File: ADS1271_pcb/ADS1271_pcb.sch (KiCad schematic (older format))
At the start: 2 parts, among them U1 ADS1271

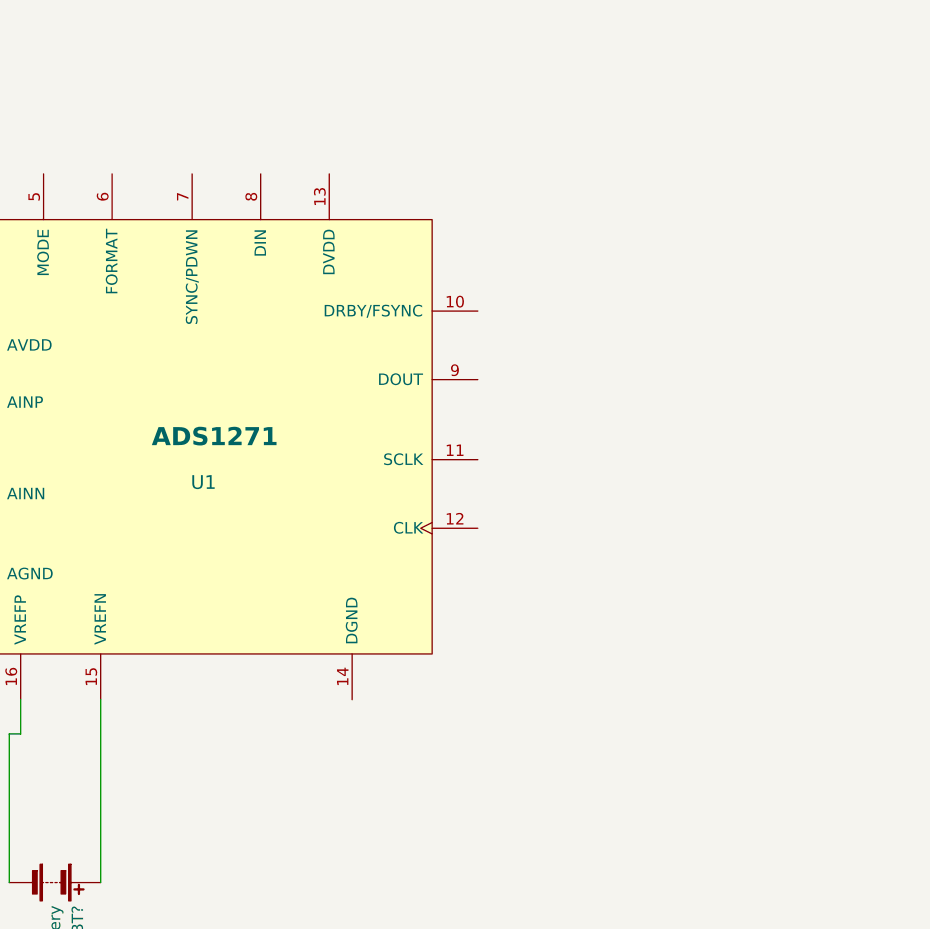
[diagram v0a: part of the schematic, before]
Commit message: Se agrega en el esquematico los labels y resistencias
FALTA: Capacitores de bypass, baterías, y definir funciones del resto de los pines. @lvillarreal
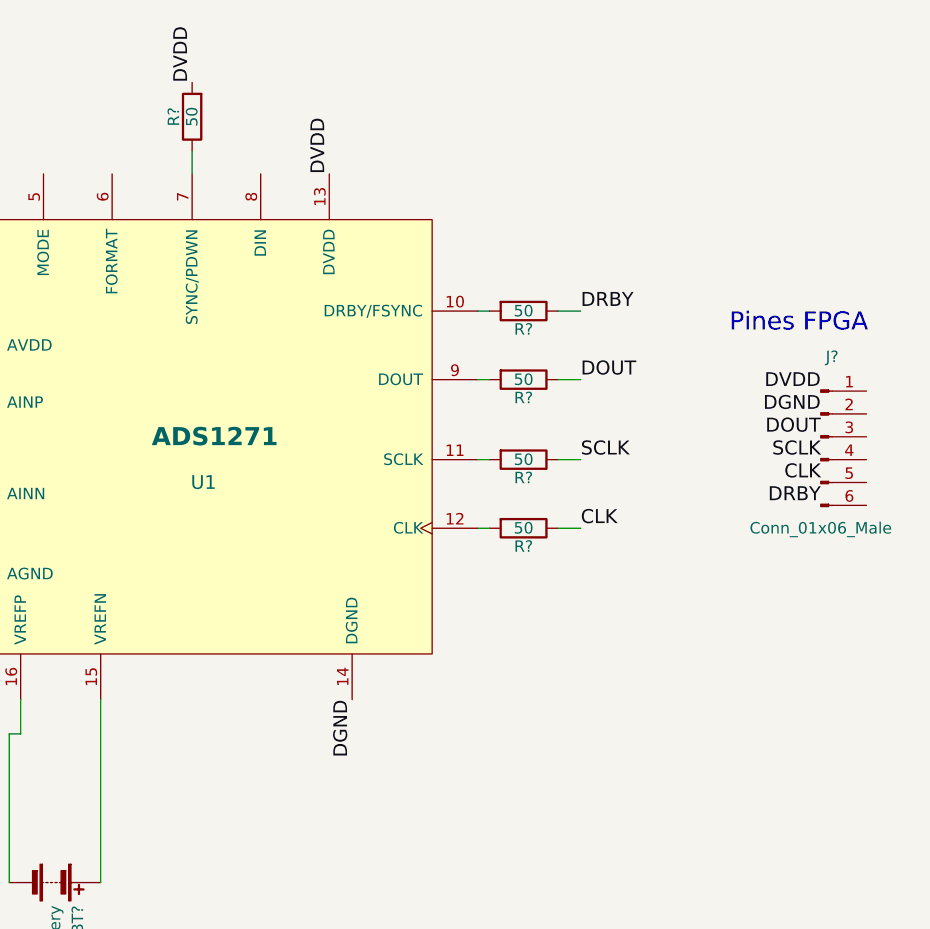
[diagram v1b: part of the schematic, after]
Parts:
- added J?: Conn_01x06_Male, symbol Conn_01x06_Male
- added R? (x5): 50, symbol R
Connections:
- net at U1.10 (DRBY/FSYNC): now also R?.2
- net at U1.11 (SCLK): now also R?.2
- net at U1.12 (CLK): now also R?.2
- net DVDD: now reaches U1.13 (DVDD)
- net DVDD: now also R?.2
- net DGND: now reaches U1.14 (DGND)
- net at U1.7 (SYNC/PDWN): now also R?.1
- net at U1.9 (DOUT): now also R?.2
- new net CLK: R?.1
- new net DOUT: R?.1
- new net DRBY: R?.1
- new net SCLK: R?.1
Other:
- note added: "Pines FPGA\n"
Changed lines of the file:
@@
 Wire Wire Line
 	3900 4350 3900 4200
+$Comp
+L Conn_01x06_Male J?
+U 1 1 5B16767B
+P 7400 3050
+F 0 "J?" H 7450 3400 50  0000 C CNN
+F 1 "Conn_01x06_Male" H 7400 2650 50  0000 C CNN
+F 2 "" H 7400 3050 50  0001 C CNN
+F 3 "" H 7400 3050 50  0001 C CNN
+	1    7400 3050
+	1    0    0    -1
+$EndComp
+Text Label 7400 2850 2    60   ~ 0
+DVDD
+Text Label 5250 1900 1    60   ~ 0
+DVDD
+Text Label 7400 2950 2    60   ~ 0
+DGND
+Text Label 5350 4200 3    60   ~ 0
+DGND
+Text Notes 7000 2600 0    79   ~ 0
+Pines FPGA\n
+Text Label 7400 3050 2    61   ~ 0
+DOUT
+Text Label 7400 3150 2    61   ~ 0
+SCLK
+Text Label 7400 3250 2    61   ~ 0
+CLK
+Text Label 7400 3350 2    61   ~ 0
+DRBY
+Text Label 6350 2500 0    61   ~ 0
+DRBY
+Text Label 6350 2800 0    61   ~ 0
+DOUT
+Text Label 6350 3150 0    61   ~ 0
+SCLK
+Text Label 6350 3450 0    61   ~ 0
+CLK
+$Comp
+L R R?
+U 1 1 5B167FA3
+P 6100 2500
+F 0 "R?" V 6180 2500 50  0000 C CNN
+F 1 "50" V 6100 2500 50  0000 C CNN
+F 2 "" V 6030 2500 50  0001 C CNN
+F 3 "" H 6100 2500 50  0001 C CNN
+	1    6100 2500
+	0    1    1    0
+$EndComp
+$Comp
+L R R?
+U 1 1 5B167FD4
+P 6100 2800
+F 0 "R?" V 6180 2800 50  0000 C CNN
+F 1 "50" V 6100 2800 50  0000 C CNN
+F 2 "" V 6030 2800 50  0001 C CNN
+F 3 "" H 6100 2800 50  0001 C CNN
+	1    6100 2800
+	0    1    1    0
+$EndComp
+$Comp
+L R R?
+U 1 1 5B1680B7
+P 6100 3150
+F 0 "R?" V 6180 3150 50  0000 C CNN
+F 1 "50" V 6100 3150 50  0000 C CNN
+F 2 "" V 6030 3150 50  0001 C CNN
+F 3 "" H 6100 3150 50  0001 C CNN
+	1    6100 3150
+	0    1    1    0
+$EndComp
+$Comp
+L R R?
+U 1 1 5B1680E5
+P 6100 3450
+F 0 "R?" V 6180 3450 50  0000 C CNN
+F 1 "50" V 6100 3450 50  0000 C CNN
+F 2 "" V 6030 3450 50  0001 C CNN
+F 3 "" H 6100 3450 50  0001 C CNN
+	1    6100 3450
+	0    1    1    0
+$EndComp
+$Comp
+L R R?
+U 1 1 5B168302
+P 4650 1650
+F 0 "R?" V 4730 1650 50  0000 C CNN
+F 1 "50" V 4650 1650 50  0000 C CNN
+F 2 "" V 4580 1650 50  0001 C CNN
+F 3 "" H 4650 1650 50  0001 C CNN
+	1    4650 1650
+	-1   0    0    1
+$EndComp
+Text Label 4650 1500 1    60   ~ 0
+DVDD
+Wire Wire Line
+	4650 1900 4650 1800
+Wire Wire Line
+	5950 2500 5900 2500
+Wire Wire Line
+	5900 2800 5950 2800
+Wire Wire Line
+	5950 3150 5900 3150
+Wire Wire Line
+	5900 3450 5950 3450
+Wire Wire Line
+	6250 3450 6350 3450
+Wire Wire Line
+	6350 3150 6250 3150
+Wire Wire Line
+	6250 2800 6350 2800
+Wire Wire Line
+	6350 2500 6250 2500
 $EndSCHEMATC

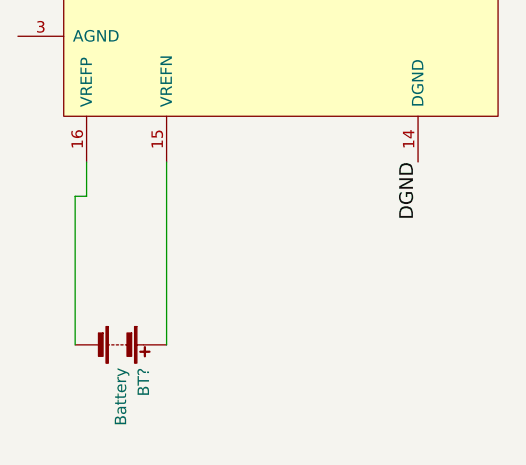
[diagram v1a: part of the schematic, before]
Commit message: Se cambia la conexión de la referencia
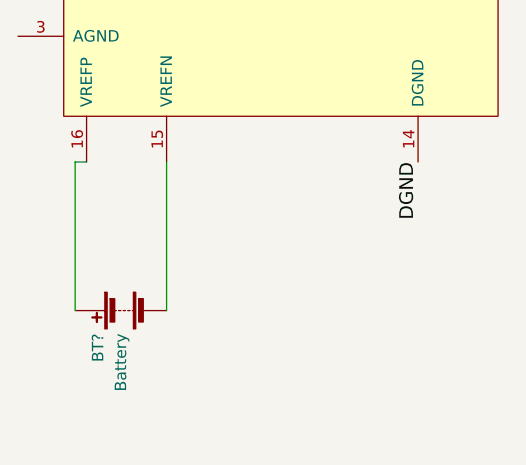
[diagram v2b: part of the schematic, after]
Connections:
- net at U1.15 (VREFN): now also BT?.2 (-); no longer BT?.1 (+)
- net at U1.16 (VREFP): now also BT?.1 (+); no longer BT?.2 (-)
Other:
- moved on the sheet: BT?
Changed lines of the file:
@@
 L Battery BT?
 U 1 1 5B1673E9
-P 4050 5000
-F 0 "BT?" H 4150 5100 50  0000 L CNN
-F 1 "Battery" H 4150 5000 50  0000 L CNN
-F 2 "" V 4050 5060 50  0001 C CNN
-F 3 "" V 4050 5060 50  0001 C CNN
-	1    4050 5000
-	0    1    1    0
+P 4050 4850
+F 0 "BT?" H 4150 4950 50  0000 L CNN
+F 1 "Battery" H 4150 4850 50  0000 L CNN
+F 2 "" V 4050 4910 50  0001 C CNN
+F 3 "" V 4050 4910 50  0001 C CNN
+	1    4050 4850
+	0    -1   1    0
 $EndComp
-Wire Wire Line
-	4250 5000 4250 4200
-Wire Wire Line
-	3850 5000 3850 4350
-Wire Wire Line
-	3850 4350 3900 4350
-Wire Wire Line
-	3900 4350 3900 4200
 $Comp
 L Conn_01x06_Male J?
@@
 Wire Wire Line
 	6350 2500 6250 2500
+Wire Wire Line
+	4250 4850 4250 4200
+Wire Wire Line
+	3850 4850 3850 4200
+Wire Wire Line
+	3850 4200 3900 4200
 $EndSCHEMATC

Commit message: Se completan los componentes basicos, expuestos en datasheet
Faltaría ver si se coloca filtro de la referencia y filtro para la entrada diferencial.
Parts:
- added C?: 1nF, symbol C
- added C? (x2): 100pF, symbol C
- added C?: 10uF, symbol C
- added C?: 100nF, symbol C
- added J?: CONN_01X02_MALE, symbol CONN_01X02_MALE
- added JP?: Jumper_NC_Dual, symbol Jumper_NC_Dual
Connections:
- net CLK: now also J?.2 (Pin_2)
- net DGND: now also J?.5 (Pin_5), U1.6 (FORMAT), U1.8 (DIN), JP?.1
- net DOUT: now also J?.4 (Pin_4)
- net DRBY: now also J?.1 (Pin_1)
- net DVDD: now also J?.6 (Pin_6), JP?.3
- net SCLK: now also J?.3 (Pin_3)
- net at U1.1 (AINP): now also C?.1, C?.1
- net at U1.2 (AINN): now also C?.1, C?.2
- net GNDA: now reaches U1.3 (AGND)
- net GNDA: now also C?.2, C?.2, C?.2, C?.2, J?.1, J?.2
- net +BATT: now reaches U1.4 (AVDD)
- net +BATT: now also C?.1, C?.1
- net at U1.5 (MODE): now also JP?.2
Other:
- note added: "Entrada analogica \nDiferencial"
- note added: "Seleccion de modo:\nDVDD -> Low Power\nDGND -> High Speed\nfloat -> High Resolution"
- moved on the sheet: J?
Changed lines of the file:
@@
 L Conn_01x06_Male J?
 U 1 1 5B16767B
-P 7400 3050
-F 0 "J?" H 7450 3400 50  0000 C CNN
-F 1 "Conn_01x06_Male" H 7400 2650 50  0000 C CNN
-F 2 "" H 7400 3050 50  0001 C CNN
-F 3 "" H 7400 3050 50  0001 C CNN
-	1    7400 3050
-	1    0    0    -1
-$EndComp
-Text Label 7400 2850 2    60   ~ 0
+P 7500 3050
+F 0 "J?" H 7550 3400 50  0000 C CNN
+F 1 "Conn_01x06_Male" H 7650 2650 50  0000 C CNN
+F 2 "" H 7500 3050 50  0001 C CNN
+F 3 "" H 7500 3050 50  0001 C CNN
+	1    7500 3050
+	1    0    0    -1
+$EndComp
+Text Label 7700 3350 0    60   ~ 0
 DVDD
 Text Label 5250 1900 1    60   ~ 0
 DVDD
-Text Label 7400 2950 2    60   ~ 0
-DGND
-Text Label 5350 4200 3    60   ~ 0
-DGND
-Text Notes 7000 2600 0    79   ~ 0
+Text Label 7700 3250 0    60   ~ 0
+DGND
+Text Notes 7350 2650 0    79   ~ 0
 Pines FPGA\n
-Text Label 7400 3050 2    61   ~ 0
+Text Label 7700 3150 0    61   ~ 0
 DOUT
-Text Label 7400 3150 2    61   ~ 0
+Text Label 7700 3050 0    61   ~ 0
 SCLK
-Text Label 7400 3250 2    61   ~ 0
+Text Label 7700 2950 0    61   ~ 0
 CLK
-Text Label 7400 3350 2    61   ~ 0
+Text Label 7700 2850 0    61   ~ 0
 DRBY
 Text Label 6350 2500 0    61   ~ 0
@@
 Text Label 4650 1500 1    60   ~ 0
 DVDD
-Wire Wire Line
-	4650 1900 4650 1800
+$Comp
+L C C?
+U 1 1 5B19F27A
+P 3450 3100
+F 0 "C?" H 3475 3200 50  0000 L CNN
+F 1 "1nF" H 3475 3000 50  0000 L CNN
+F 2 "" H 3488 2950 50  0001 C CNN
+F 3 "" H 3450 3100 50  0001 C CNN
+	1    3450 3100
+	1    0    0    -1
+$EndComp
+$Comp
+L GNDA #PWR?
+U 1 1 5B1A1201
+P 2850 3000
+F 0 "#PWR?" H 2850 2750 50  0001 C CNN
+F 1 "GNDA" H 2850 2850 50  0000 C CNN
+F 2 "" H 2850 3000 50  0001 C CNN
+F 3 "" H 2850 3000 50  0001 C CNN
+	1    2850 3000
+	1    0    0    -1
+$EndComp
+$Comp
+L C C?
+U 1 1 5B1A1242
+P 3150 2900
+F 0 "C?" H 3175 3000 50  0000 L CNN
+F 1 "100pF" H 3175 2800 50  0000 L CNN
+F 2 "" H 3188 2750 50  0001 C CNN
+F 3 "" H 3150 2900 50  0001 C CNN
+	1    3150 2900
+	0    1    1    0
+$EndComp
+$Comp
+L C C?
+U 1 1 5B1A185C
+P 3150 3300
+F 0 "C?" H 3175 3400 50  0000 L CNN
+F 1 "100pF" H 3175 3200 50  0000 L CNN
+F 2 "" H 3188 3150 50  0001 C CNN
+F 3 "" H 3150 3300 50  0001 C CNN
+	1    3150 3300
+	0    1    1    0
+$EndComp
+$Comp
+L GNDA #PWR?
+U 1 1 5B1A18FF
+P 2850 3400
+F 0 "#PWR?" H 2850 3150 50  0001 C CNN
+F 1 "GNDA" H 2850 3250 50  0000 C CNN
+F 2 "" H 2850 3400 50  0001 C CNN
+F 3 "" H 2850 3400 50  0001 C CNN
+	1    2850 3400
+	1    0    0    -1
+$EndComp
+$Comp
+L GNDA #PWR?
+U 1 1 5B1A6982
+P 3500 3750
+F 0 "#PWR?" H 3500 3500 50  0001 C CNN
+F 1 "GNDA" H 3500 3600 50  0000 C CNN
+F 2 "" H 3500 3750 50  0001 C CNN
+F 3 "" H 3500 3750 50  0001 C CNN
+	1    3500 3750
+	1    0    0    -1
+$EndComp
+Text Label 5350 4200 3    60   ~ 0
+DGND
+$Comp
+L C C?
+U 1 1 5B1AB96E
+P 3300 2450
+F 0 "C?" H 3325 2550 50  0000 L CNN
+F 1 "10uF" H 3325 2350 50  0000 L CNN
+F 2 "" H 3338 2300 50  0001 C CNN
+F 3 "" H 3300 2450 50  0001 C CNN
+	1    3300 2450
+	0    1    1    0
+$EndComp
+$Comp
+L C C?
+U 1 1 5B1ABAA9
+P 3300 2150
+F 0 "C?" H 3325 2250 50  0000 L CNN
+F 1 "100nF" H 3325 2050 50  0000 L CNN
+F 2 "" H 3338 2000 50  0001 C CNN
+F 3 "" H 3300 2150 50  0001 C CNN
+	1    3300 2150
+	0    1    1    0
+$EndComp
 Wire Wire Line
 	5950 2500 5900 2500
@@
 Wire Wire Line
 	3850 4200 3900 4200
+Wire Wire Line
+	3300 3300 3600 3300
+Wire Wire Line
+	3450 3300 3450 3250
+Wire Wire Line
+	3300 2900 3600 2900
+Wire Wire Line
+	3450 2900 3450 2950
+Wire Wire Line
+	2600 2900 3000 2900
+Wire Wire Line
+	2850 2900 2850 3000
+Connection ~ 3450 2900
+Connection ~ 3450 3300
+Wire Wire Line
+	2600 3300 3000 3300
+Wire Wire Line
+	2850 3300 2850 3400
+Wire Wire Line
+	2350 3050 2600 3050
+Wire Wire Line
+	2600 3050 2600 2900
+Connection ~ 2850 2900
+Wire Wire Line
+	2350 3250 2600 3250
+Wire Wire Line
+	2600 3250 2600 3300
+Connection ~ 2850 3300
+Wire Wire Line
+	3500 3750 3500 3650
+Wire Wire Line
+	3500 3650 3600 3650
+Wire Wire Line
+	3450 2450 3550 2450
+Wire Wire Line
+	3550 1800 3550 2650
+Wire Wire Line
+	3550 2650 3600 2650
+Wire Wire Line
+	3550 2150 3450 2150
+Connection ~ 3550 2450
+$Comp
+L GNDA #PWR?
+U 1 1 5B1ADA12
+P 3000 2600
+F 0 "#PWR?" H 3000 2350 50  0001 C CNN
+F 1 "GNDA" H 3000 2450 50  0000 C CNN
+F 2 "" H 3000 2600 50  0001 C CNN
+F 3 "" H 3000 2600 50  0001 C CNN
+	1    3000 2600
+	1    0    0    -1
+$EndComp
+$Comp
+L GNDA #PWR?
+U 1 1 5B1ADA7F
+P 3000 2250
+F 0 "#PWR?" H 3000 2000 50  0001 C CNN
+F 1 "GNDA" H 3000 2100 50  0000 C CNN
+F 2 "" H 3000 2250 50  0001 C CNN
+F 3 "" H 3000 2250 50  0001 C CNN
+	1    3000 2250
+	1    0    0    -1
+$EndComp
+Wire Wire Line
+	3150 2450 3000 2450
+Wire Wire Line
+	3000 2450 3000 2600
+Wire Wire Line
+	3150 2150 3000 2150
+Wire Wire Line
+	3000 2150 3000 2250
+$Comp
+L +BATT #PWR?
+U 1 1 5B1AF906
+P 3550 1800
+F 0 "#PWR?" H 3550 1650 50  0001 C CNN
+F 1 "+BATT" H 3550 1940 50  0000 C CNN
+F 2 "" H 3550 1800 50  0001 C CNN
+F 3 "" H 3550 1800 50  0001 C CNN
+	1    3550 1800
+	1    0    0    -1
+$EndComp
+Connection ~ 3550 2150
+$Comp
+L Jumper_NC_Dual JP?
+U 1 1 5B1B102E
+P 4000 1150
+F 0 "JP?" H 4050 1050 50  0000 L CNN
+F 1 "Jumper_NC_Dual" H 4000 1250 50  0000 C BNN
+F 2 "" H 4000 1150 50  0001 C CNN
+F 3 "" H 4000 1150 50  0001 C CNN
+	1    4000 1150
+	1    0    0    -1
+$EndComp
+Text Label 4250 1150 0    60   ~ 0
+DVDD
+Text Label 3750 1150 2    60   ~ 0
+DGND
+Wire Wire Line
+	4000 1250 4000 1900
+Text Label 4300 1900 1    60   ~ 0
+DGND
+Text Label 4950 1900 1    60   ~ 0
+DGND
+$Comp
+L CONN_01X02_MALE J?
+U 1 1 5B1A4D1B
+P 2050 3150
+F 0 "J?" H 2050 3325 50  0000 C CNN
+F 1 "CONN_01X02_MALE" H 2050 2950 50  0000 C CNN
+F 2 "" H 2050 3250 50  0001 C CNN
+F 3 "" H 2050 3250 50  0001 C CNN
+	1    2050 3150
+	1    0    0    -1
+$EndComp
+Wire Wire Line
+	4650 1800 4650 1900
+Text Notes 1000 3200 0    60   ~ 0
+Entrada analogica \nDiferencial
+Text Notes 3500 950  0    60   ~ 0
+Seleccion de modo:\nDVDD -> Low Power\nDGND -> High Speed\nfloat -> High Resolution
 $EndSCHEMATC

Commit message: Cambios en los capacitores en líneas diferenciales analogicas
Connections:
- net GNDA: now also C?.1, C?.1; no longer C?.2, C?.2, J?.1, J?.2
- net at C?.1, U1.1 (AINP): now also C?.2, J?.1; no longer C?.1
- net at C?.2, U1.2 (AINN): now also C?.2, J?.2; no longer C?.1
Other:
- note added: "08/06/18\n"
- note added: "Analizar alimentación analógica: Como la implementamos? Bateria, con tensión regulada?\n"
- note added: "PCB prueba para ADC ADS1271\n"
- note added: "V 0.2\n"
- moved on the sheet: C?
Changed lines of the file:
@@
 L GNDA #PWR?
 U 1 1 5B1A1201
-P 2850 3000
-F 0 "#PWR?" H 2850 2750 50  0001 C CNN
-F 1 "GNDA" H 2850 2850 50  0000 C CNN
-F 2 "" H 2850 3000 50  0001 C CNN
-F 3 "" H 2850 3000 50  0001 C CNN
-	1    2850 3000
+P 2800 3700
+F 0 "#PWR?" H 2800 3450 50  0001 C CNN
+F 1 "GNDA" H 2800 3550 50  0000 C CNN
+F 2 "" H 2800 3700 50  0001 C CNN
+F 3 "" H 2800 3700 50  0001 C CNN
+	1    2800 3700
 	1    0    0    -1
 $EndComp
@@
 L C C?
 U 1 1 5B1A1242
-P 3150 2900
-F 0 "C?" H 3175 3000 50  0000 L CNN
-F 1 "100pF" H 3175 2800 50  0000 L CNN
-F 2 "" H 3188 2750 50  0001 C CNN
-F 3 "" H 3150 2900 50  0001 C CNN
-	1    3150 2900
-	0    1    1    0
+P 2800 3550
+F 0 "C?" H 2825 3650 50  0000 L CNN
+F 1 "100pF" H 2900 3550 50  0000 L CNN
+F 2 "" H 2838 3400 50  0001 C CNN
+F 3 "" H 2800 3550 50  0001 C CNN
+	1    2800 3550
+	-1   0    0    1
 $EndComp
 $Comp
 L C C?
 U 1 1 5B1A185C
-P 3150 3300
-F 0 "C?" H 3175 3400 50  0000 L CNN
-F 1 "100pF" H 3175 3200 50  0000 L CNN
-F 2 "" H 3188 3150 50  0001 C CNN
-F 3 "" H 3150 3300 50  0001 C CNN
-	1    3150 3300
-	0    1    1    0
+P 3150 3550
+F 0 "C?" H 3175 3650 50  0000 L CNN
+F 1 "100pF" H 2800 3550 50  0000 L CNN
+F 2 "" H 3188 3400 50  0001 C CNN
+F 3 "" H 3150 3550 50  0001 C CNN
+	1    3150 3550
+	-1   0    0    1
 $EndComp
 $Comp
 L GNDA #PWR?
 U 1 1 5B1A18FF
-P 2850 3400
-F 0 "#PWR?" H 2850 3150 50  0001 C CNN
-F 1 "GNDA" H 2850 3250 50  0000 C CNN
-F 2 "" H 2850 3400 50  0001 C CNN
-F 3 "" H 2850 3400 50  0001 C CNN
-	1    2850 3400
+P 3150 3700
+F 0 "#PWR?" H 3150 3450 50  0001 C CNN
+F 1 "GNDA" H 3150 3550 50  0000 C CNN
+F 2 "" H 3150 3700 50  0001 C CNN
+F 3 "" H 3150 3700 50  0001 C CNN
+	1    3150 3700
 	1    0    0    -1
 $EndComp
@@
 	3850 4200 3900 4200
 Wire Wire Line
-	3300 3300 3600 3300
+	2600 3300 3600 3300
 Wire Wire Line
 	3450 3300 3450 3250
 Wire Wire Line
-	3300 2900 3600 2900
+	2600 2900 3600 2900
 Wire Wire Line
 	3450 2900 3450 2950
-Wire Wire Line
-	2600 2900 3000 2900
-Wire Wire Line
-	2850 2900 2850 3000
 Connection ~ 3450 2900
 Connection ~ 3450 3300
 Wire Wire Line
-	2600 3300 3000 3300
-Wire Wire Line
-	2850 3300 2850 3400
-Wire Wire Line
 	2350 3050 2600 3050
 Wire Wire Line
 	2600 3050 2600 2900
-Connection ~ 2850 2900
+Connection ~ 2800 2900
 Wire Wire Line
 	2350 3250 2600 3250
 Wire Wire Line
 	2600 3250 2600 3300
-Connection ~ 2850 3300
 Wire Wire Line
 	3500 3750 3500 3650
@@
 	3500 3650 3600 3650
 Wire Wire Line
-	3450 2450 3550 2450
+	3550 2450 3450 2450
 Wire Wire Line
 	3550 1800 3550 2650
@@
 Text Notes 3500 950  0    60   ~ 0
 Seleccion de modo:\nDVDD -> Low Power\nDGND -> High Speed\nfloat -> High Resolution
+Connection ~ 3150 3300
+Wire Wire Line
+	3150 3300 3150 3400
+Wire Wire Line
+	2800 2900 2800 3400
+Text Notes 2600 5350 0    60   ~ 0
+Analizar alimentación analógica: Como la implementamos? Bateria, con tensión regulada?\n
+Text Notes 7400 7500 0    60   ~ 0
+PCB prueba para ADC ADS1271\n
+Text Notes 10600 7650 0    60   ~ 0
+V 0.2\n
+Text Notes 8150 7650 0    60   ~ 0
+08/06/18\n
 $EndSCHEMATC
